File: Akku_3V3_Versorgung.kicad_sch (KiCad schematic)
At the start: 29 parts, among them J1 Conn_01x03, P1 USB_C_Plug_USB2.0, Q1 FS8205A, U1 TP4056, U2 DW01A, U3 MT3608, U4 AP2112K-3.3

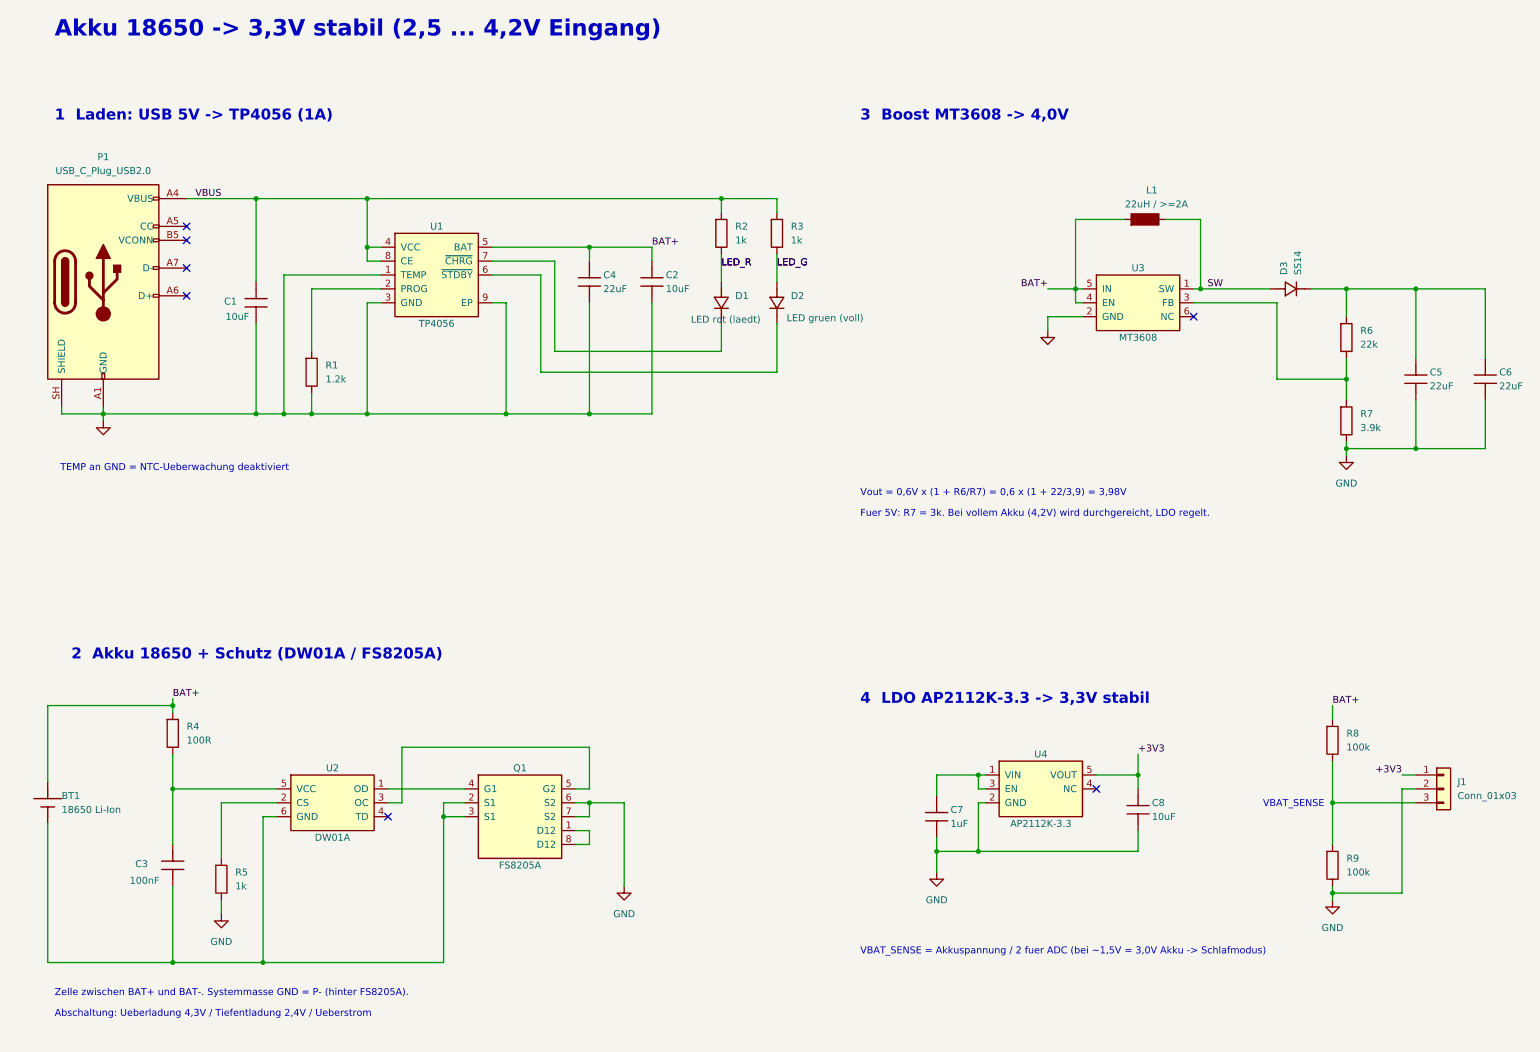
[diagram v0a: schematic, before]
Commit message: Schaltplan-Korrekturen nach Datenblatt-Review
- LDO-Eingang (U4) mit Boost-Ausgang verbunden (Netz VBOOST), vorher
  ohne Verbindung
- USB-C: Buchsen-Symbol statt Stecker (passend zu Footprint USB4105),
  CC1/CC2 je 5,1k (R10/R11) nach GND, D+/D-/SBU als No-Connect
- P1/J1-Symbole in die Projektbibliothek Akku3V3 uebernommen
- Netz VBAT_SENSE benannt
- Notiztexte an Datenblaetter angeglichen (Ladestrom 0,9A bei 1,2k,
  Eingangsbereich ab 2,4V, Boost-Verhalten bei vollem Akku)
- README an Schaltplan angepasst
- Platine geleert (Neuanfang Layout)

Co-Authored-By: Claude Opus 5.5 <noreply@anthropic.com>
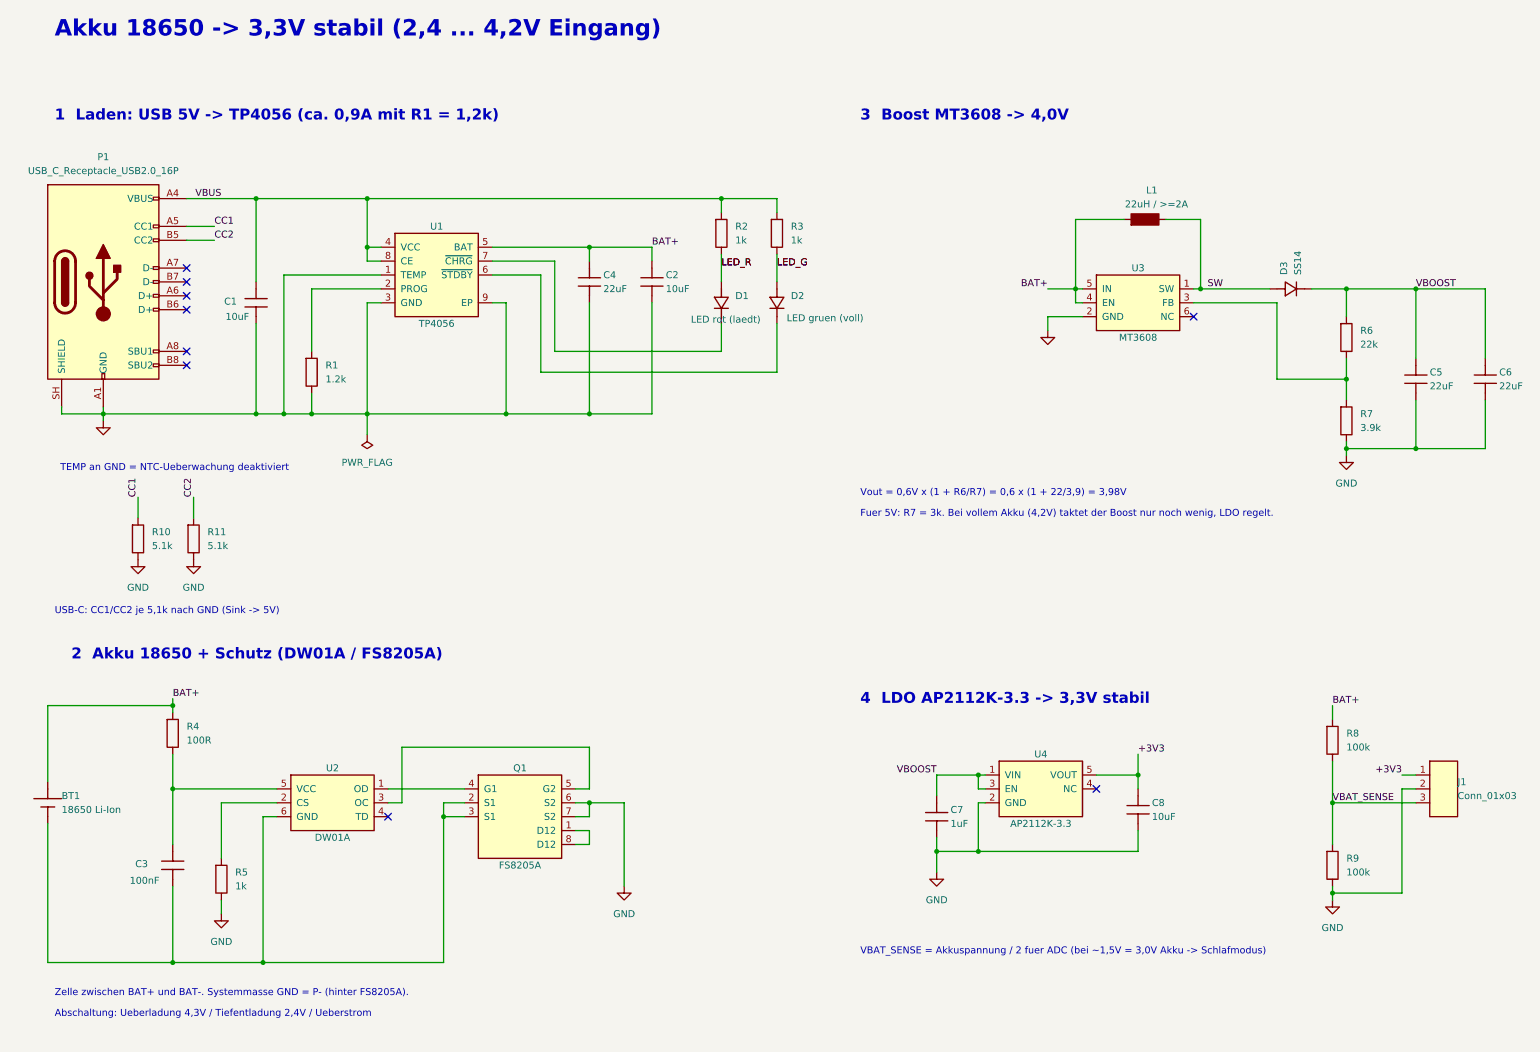
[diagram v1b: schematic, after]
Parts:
- added R10, R11: 5.1k, Resistor_SMD:R_1206_3216Metric, symbol Akku3V3:R
- J1: symbol Connector_Generic:Conn_01x03 -> Akku3V3:Conn_01x03
- P1: value USB_C_Plug_USB2.0 -> USB_C_Receptacle_USB2.0_16P; symbol Connector:USB_C_Plug_USB2.0 -> Akku3V3:USB_C_Receptacle_USB2.0_16P
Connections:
- net GND: now also R10.2, R11.2
- net VBOOST: now reaches C5.1, C6.1, D3.1 (K), R6.1
- net VBOOST: now also C7.1, U4.1 (VIN), U4.3 (EN)
- net CC1: now reaches P1.A5 (CC1)
- net CC1: now also R10.1
- net CC2: now reaches P1.B5 (CC2)
- net CC2: now also R11.1
- net VBAT_SENSE: now reaches J1.3 (Pin_3), R8.2, R9.1
- no-connect marks 7 -> 9
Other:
- note added: "1 Laden: USB 5V -> TP4056 (ca. 0,9A mit R1 = 1,2k)"
- note added: "Akku 18650 -> 3,3V stabil (2,4 ... 4,2V Eingang)"
- note added: "Fuer 5V: R7 = 3k. Bei vollem Akku (4,2V) taktet der Boost nur noch wenig, LDO regelt."
- note added: "USB-C: CC1/CC2 je 5,1k nach GND (Sink -> 5V)"
- note removed: "1 Laden: USB 5V -> TP4056 (1A)"
- note removed: "Akku 18650 -> 3,3V stabil (2,5 ... 4,2V Eingang)"
- note removed: "Fuer 5V: R7 = 3k. Bei vollem Akku (4,2V) wird durchgereicht, LDO regelt."
- note removed: "VBAT_SENSE"

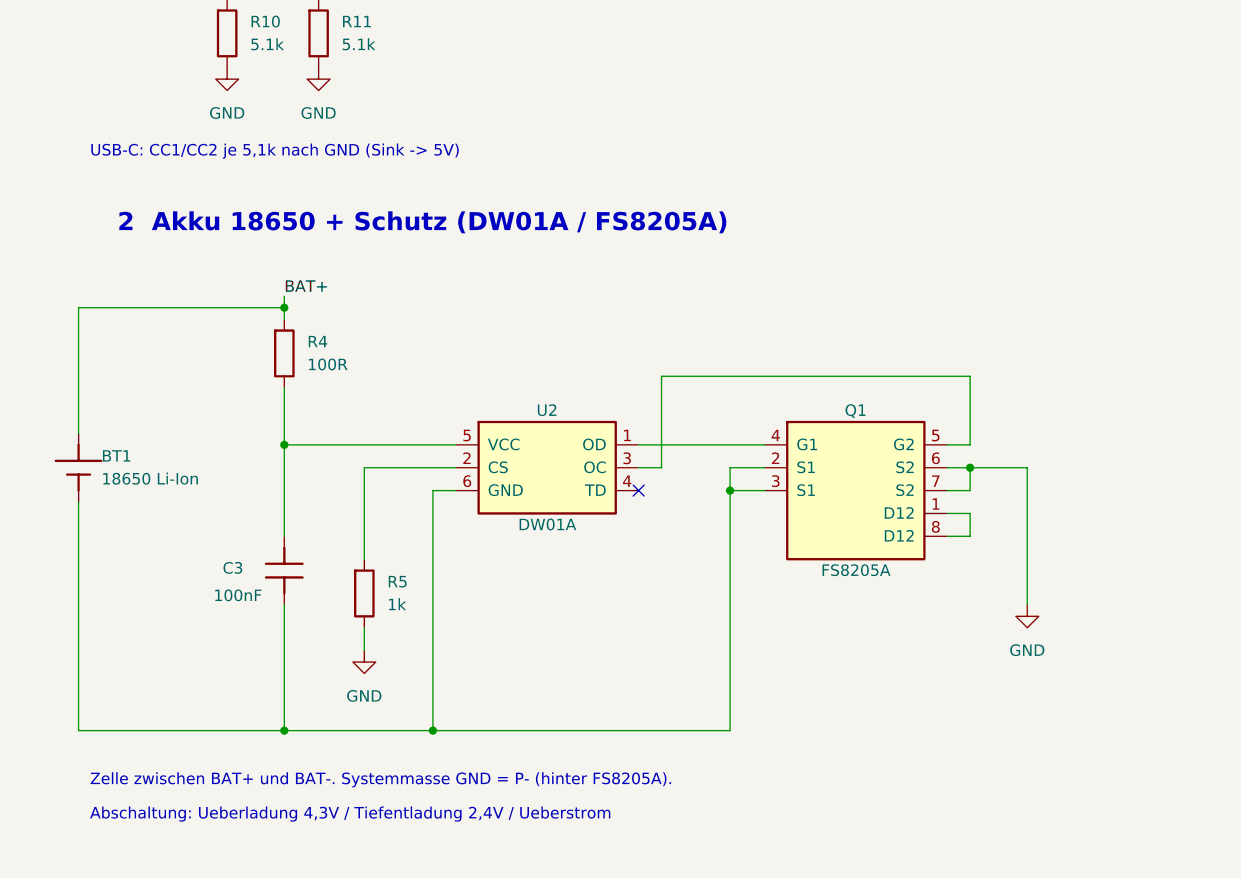
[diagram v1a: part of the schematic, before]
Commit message: DW01A auf KiCad-Standardsymbol (U5), PWR_FLAGs für ERC
- DW01A nutzt jetzt Battery_Management:DW01A, Referenz U5 (Netzliste unverändert)
- PWR_FLAGs an U5-VCC und BAT− ergänzt, ERC ohne Fehler
- README: U2 → U5
- CLAUDE.md: Regel "alle Symbole aus Akku3V3:*" entfernt

Co-Authored-By: Claude Opus 5.5 <noreply@anthropic.com>
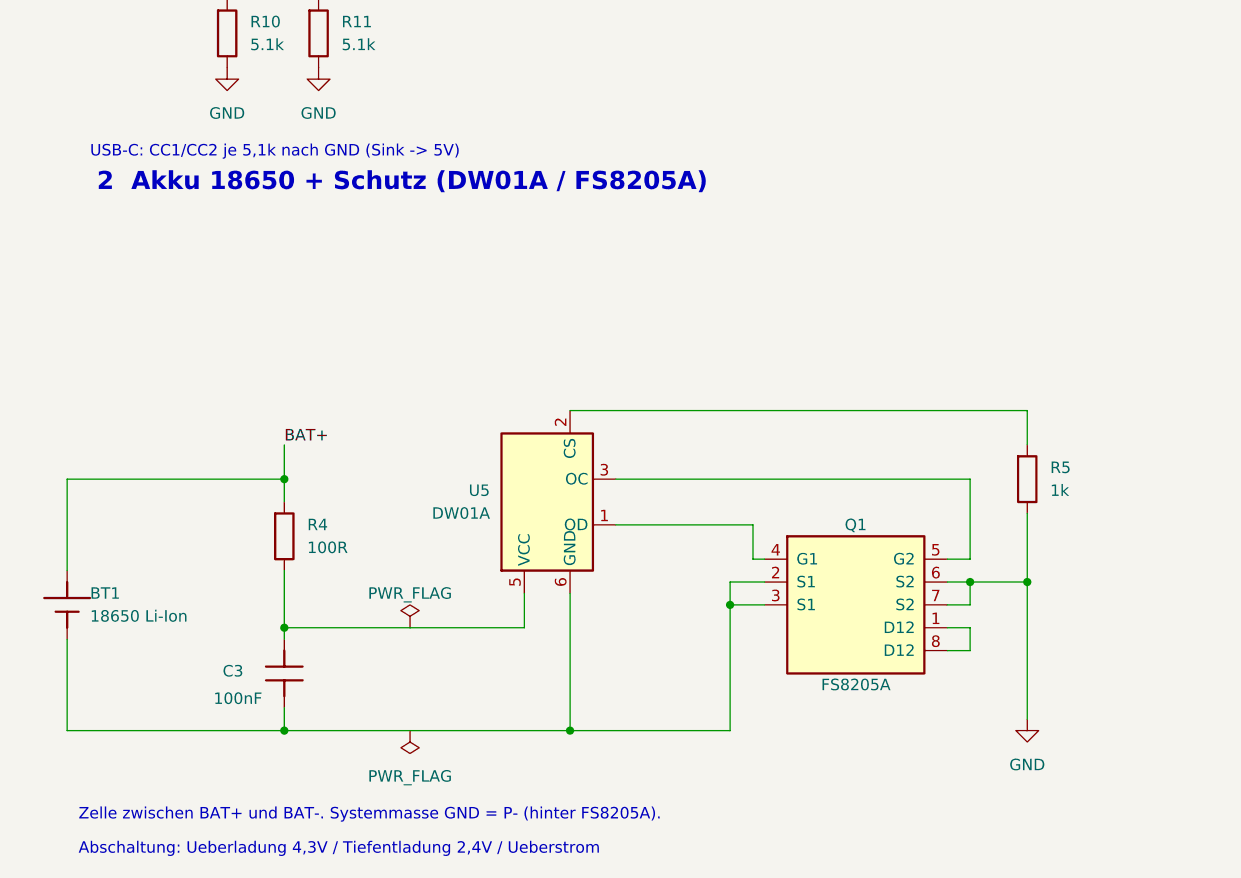
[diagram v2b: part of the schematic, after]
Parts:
- removed U2: DW01A, Package_TO_SOT_SMD:SOT-23-6, symbol Akku3V3:DW01A
- added U5: DW01A, Package_TO_SOT_SMD:SOT-23-6, symbol Battery_Management:DW01A
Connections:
- net at C3.1, R4.2: now also U5.5 (VCC)
- net at BT1.2 (-), C3.2, Q1.2 (S1)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: now also U5.6 (GND)
- net at Q1.4 (G1): now also U5.1 (OD)
- net at R5.1: now also U5.2 (CS)
- net at Q1.5 (G2): now also U5.3 (OC)
- no-connect marks 9 -> 8
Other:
- moved on the sheet: BT1, C3, Q1, R4, R5
